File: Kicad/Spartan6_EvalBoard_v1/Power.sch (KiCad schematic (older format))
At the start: 0 parts

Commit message: Schematic almost done
Schematic almost done, just to connect connector to FPGA
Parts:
- added C1, C11, C12, C5, C7, C8: 10u, ~, symbol C
- added C10, C9: 470p, ~, symbol C
- added C2, C3: 1u, ~, symbol C
- added C4: 3.3n, ~, symbol C
- added C6: 100n, ~, symbol C
- added D1: RED, ~, symbol LED
- added D2: GREEN, ~, symbol LED
- added D3, D4, D5, D6, D7: ORANGE, ~, symbol LED
- added FB?: F, ~, symbol F
- added JP1, JP2: JUMPER3, ~, symbol JUMPER3
- added L1: 18u, ~, symbol INDUCTOR
- added P1: CONN_2, symbol CONN_2
- added PS1: MAX1750X, symbol MAX1750X
- added PS2, PS3: LMZ1050X, ~, symbol LMZ1050X
- added Q3: MOSFET_N, ~, symbol MOSFET_N
- added R10, R12, R2, R4, R7, R8, R9: 1.2k, ~, symbol R
- added R11: 4.7k, ~, symbol R
- added R13, R15: 120k, ~, symbol R
- added R14: 154k, ~, symbol R
- added R16: 30.9k, ~, symbol R
- added R5: 10k, ~, symbol R
- added R6: 47k, ~, symbol R
- added X?: USBMICRO, symbol USBMICRO
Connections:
- net labels added: +1.2V, +3.3V, +5V, 5V_RDY, 5V_SWITCHER, 5V_SW_RDY, 5V_USB, GND, LED1, LED2, LED3, LED4, VCC
- wire segments 0 -> 128
- no-connect marks 0 -> 4
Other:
- note added: "4.7k*100n=470us to reach 63% of 5V"
- note added: "User the right transistor"

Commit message: Schematic and netllist created
The correct fpga connection to connector will have to be carried out.
Some more footprints need to be created.
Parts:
- P1: value CONN_2 -> PWR
- gave numbers to parts that had none: 2
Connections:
- net labels added: 1.2V, 3.3V, 5V
- net labels removed: +1.2V, +3.3V, +5V
- wire segments 128 -> 131
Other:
- moved on the sheet: C1, C2, C3, C4, C5, C6, D1, D2, D3, FB301, JP1, JP2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

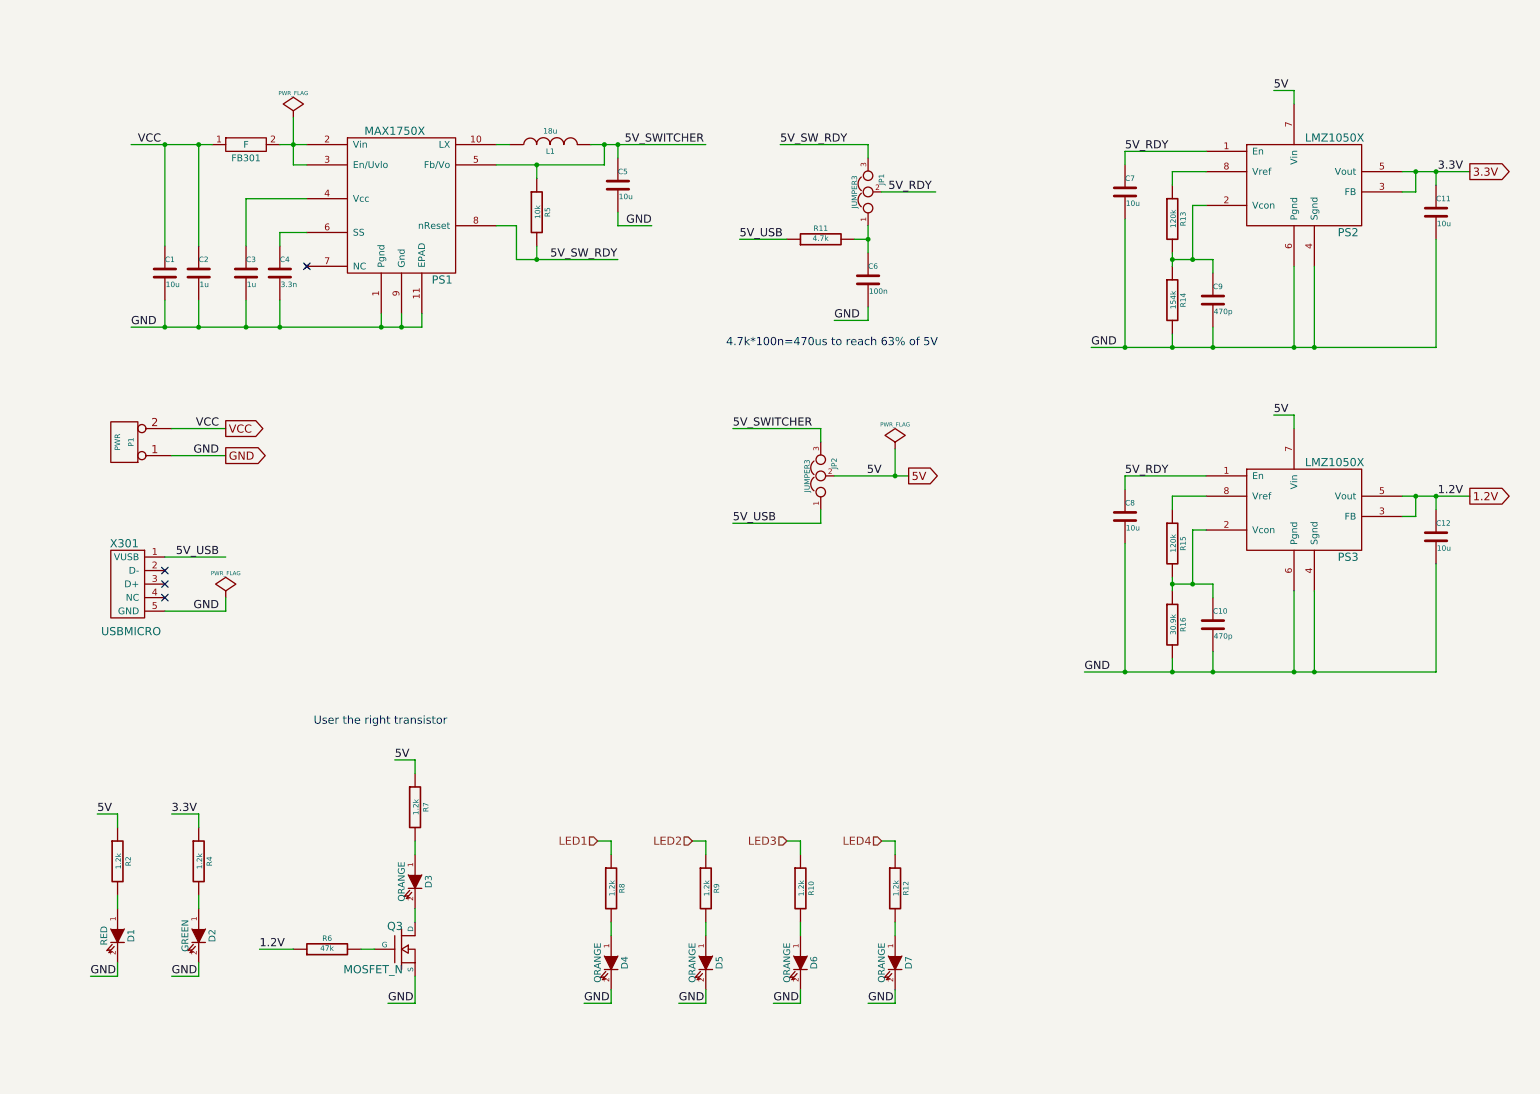
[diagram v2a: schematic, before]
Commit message: Schematic completed, layout starte
Schematic completed, layout starte
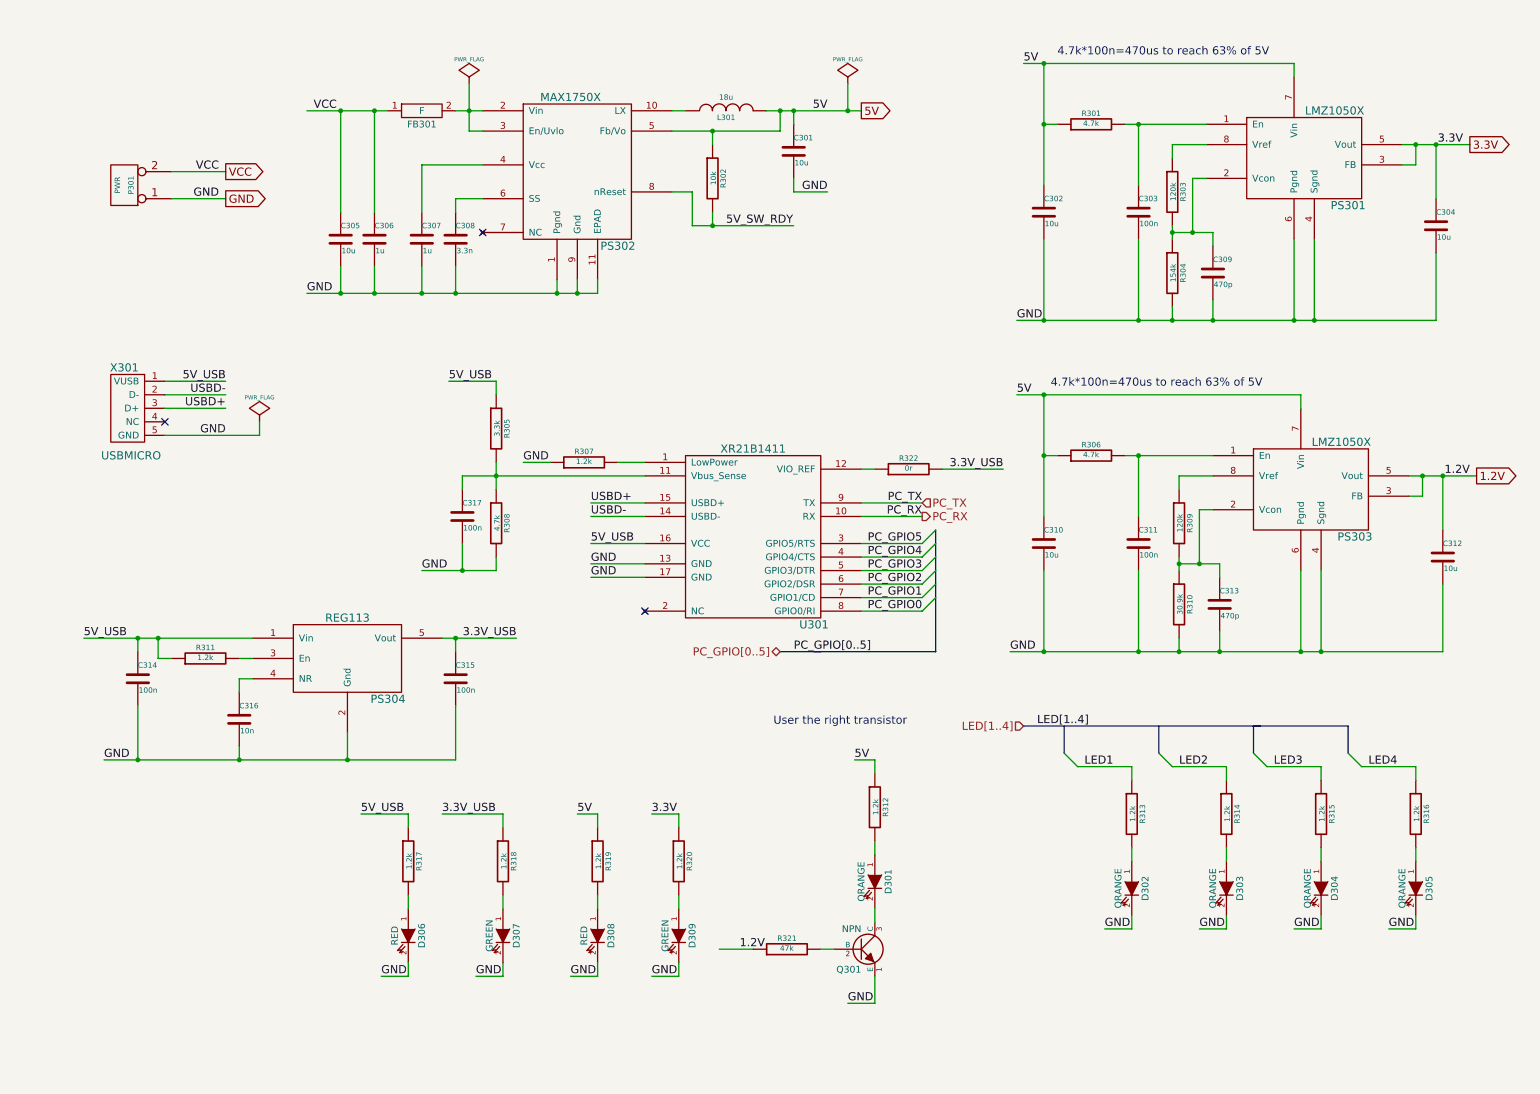
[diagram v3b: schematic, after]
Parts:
- removed C6: 100n, ~, symbol C
- removed C7, C8: 10u, ~, symbol C
- removed JP1, JP2: JUMPER3, ~, symbol JUMPER3
- removed Q3: MOSFET_N, ~, symbol MOSFET_N
- removed R11: 4.7k, ~, symbol R
- added C302, C310: 10u, ~, symbol C
- added C303, C311, C314, C315, C317: 100n, ~, symbol C
- added C316: 10n, ~, symbol C
- added D306: RED, ~, symbol LED
- added D307: GREEN, ~, symbol LED
- added PS304: REG113, ~, symbol REG113
- added Q301: NPN, ~, symbol NPN
- added R301, R306, R308: 4.7k, ~, symbol R
- added R305: 3.3k, ~, symbol R
- added R307, R311, R317, R318: 1.2k, ~, symbol R
- added R322: 0r, ~, symbol R
- added U301: XR21B1411, symbol XR21B1411
- renumbered C5 to C301, C11 to C304, C1 to C305, C2 to C306, C3 to C307, C4 to C308, C9 to C309, C12 to C312, C10 to C313, D3 to D301, D4 to D302, D5 to D303, D6 to D304, D7 to D305, D1 to D308, D2 to D309, L1 to L301, P1 to P301, PS2 to PS301, PS1 to PS302, PS3 to PS303, R5 to R302, R13 to R303, R14 to R304, R15 to R309, R16 to R310, R7 to R312, R8 to R313, R9 to R314, R10 to R315, R12 to R316, R2 to R319, R4 to R320, R6 to R321
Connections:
- net labels added: 3.3V_USB, LED[1..4], PC_GPIO0, PC_GPIO1, PC_GPIO2, PC_GPIO3, PC_GPIO4, PC_GPIO5, PC_GPIO[0..5], PC_RX, PC_TX, USBD+, USBD-
- net labels removed: 5V_RDY, 5V_SWITCHER
- wire segments 131 -> 175
- no-connect marks 4 -> 3
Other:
- moved on the sheet: C301, C304, C305, C306, C307, C308, C309, C312, C313, D301, D302, D303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

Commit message: BZR - Layout half done
Using LaunchPad Kicad
Layout more than half completed
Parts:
- C301, C302, C304, C305, C310, C312, C316: footprint ~ -> Capacitors_SMD.pretty:C_0603
- C303, C306, C307, C308, C309, C311, C313, C314, C315, C317, FB301: footprint ~ -> Capacitors_SMD.pretty:C_0402
- D301, D302, D303, D304, D305, D306, D307, D308, D309: footprint ~ -> LEDs.pretty:LED-0603
- L301: footprint ~ -> Eric.mod:IND6x6
- P301: footprint (none) -> Connect.pretty:bornier2
- PS301, PS303: footprint ~ -> Eric.mod:SIL08
- PS302: footprint (none) -> Eric.mod:TDFN10
- PS304: footprint ~ -> tinkerforge.mod:SOT23-5
- Q301: footprint ~ -> Eric.mod:TSLP-3-1
- R301, R302, R303, R304, R305, R306, R307, R308, R309, R310, R311, R312, R313, R314, R315, R316, R317, R318, R319, R320, R321, R322: footprint ~ -> Resistors_SMD.pretty:R_0402
- U301: footprint (none) -> Eric.mod:QFN-16
- X301: footprint (none) -> tinkerforge.mod:USB-MINI-B-SMD

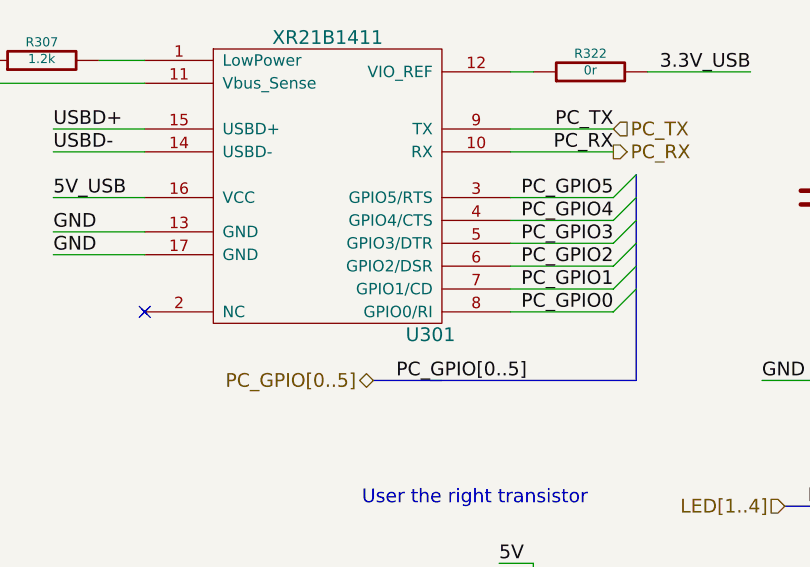
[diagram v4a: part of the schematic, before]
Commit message: Layout completed, just need to run DRC.
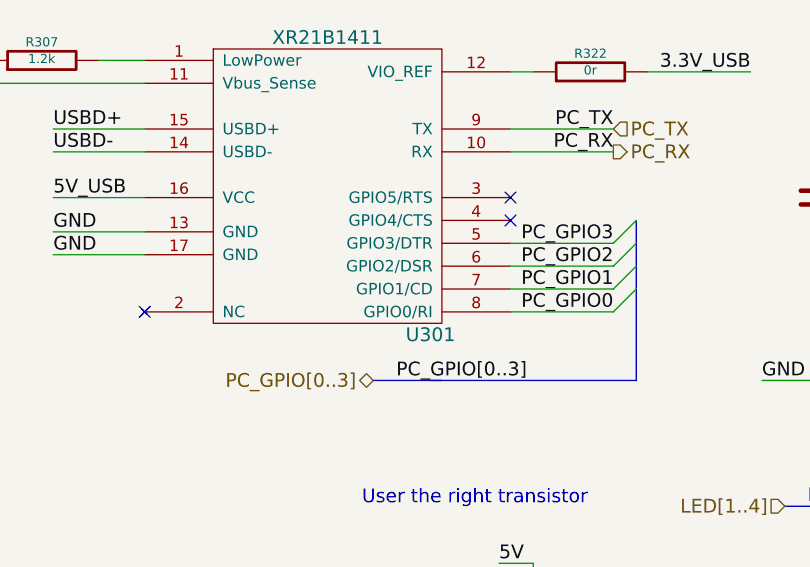
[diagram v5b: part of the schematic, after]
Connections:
- net PC_GPIO4: no longer names the net of U301.4 (GPIO4/CTS)
- net PC_GPIO5: no longer names the net of U301.3 (GPIO5/RTS)
- no-connect marks 3 -> 5
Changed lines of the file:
@@
 Text Label 6800 4050 2    60   ~ 0
 PC_RX
-Text Label 6800 4250 2    60   ~ 0
-PC_GPIO5
-Text Label 6800 4350 2    60   ~ 0
-PC_GPIO4
 Text Label 6800 4450 2    60   ~ 0
 PC_GPIO3
@@
 PC_GPIO0
 Text Label 5850 5050 0    60   ~ 0
-PC_GPIO[0..5]
+PC_GPIO[0..3]
 $Comp
 L R R307
@@
 5V_USB
 Text HLabel 5750 5050 0    60   BiDi ~ 0
-PC_GPIO[0..5]
+PC_GPIO[0..3]
 Text HLabel 6800 3950 2    60   Input ~ 0
 PC_TX
@@
 	6350 4050 6800 4050
 Wire Wire Line
-	6350 4250 6800 4250
-Wire Wire Line
-	6350 4350 6800 4350
-Wire Wire Line
 	6350 4450 6800 4450
 Wire Wire Line
@@
 	6350 4750 6800 4750
 Wire Bus Line
-	6900 4150 6900 5050
+	6900 4350 6900 5050
 Wire Bus Line
 	6900 5050 6000 5050
@@
 Connection ~ 1150 4950
 Entry Wire Line
-	6800 4250 6900 4150
-Entry Wire Line
-	6800 4350 6900 4250
-Entry Wire Line
 	6800 4450 6900 4350
 Entry Wire Line
@@
 	1    0    0    -1
 $EndComp
+NoConn ~ 6350 4250
+NoConn ~ 6350 4350
 $EndSCHEMATC
